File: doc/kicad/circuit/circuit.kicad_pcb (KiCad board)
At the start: 2 copper layers, 45.5 x 53.1 mm, 17 parts, among them J1 4X4 Button Matrix, J1.1 2X2 Button Matrix A, J1.1.1 Button 1, J1.1.2 Button 2, J1.1.3 Button 5, J1.1.4 Button 6, J1.2 2X2 Button Matrix B, J1.2.1 Button 3, J1.2.2 Button 4, J1.3 2X2 Button Matrix C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

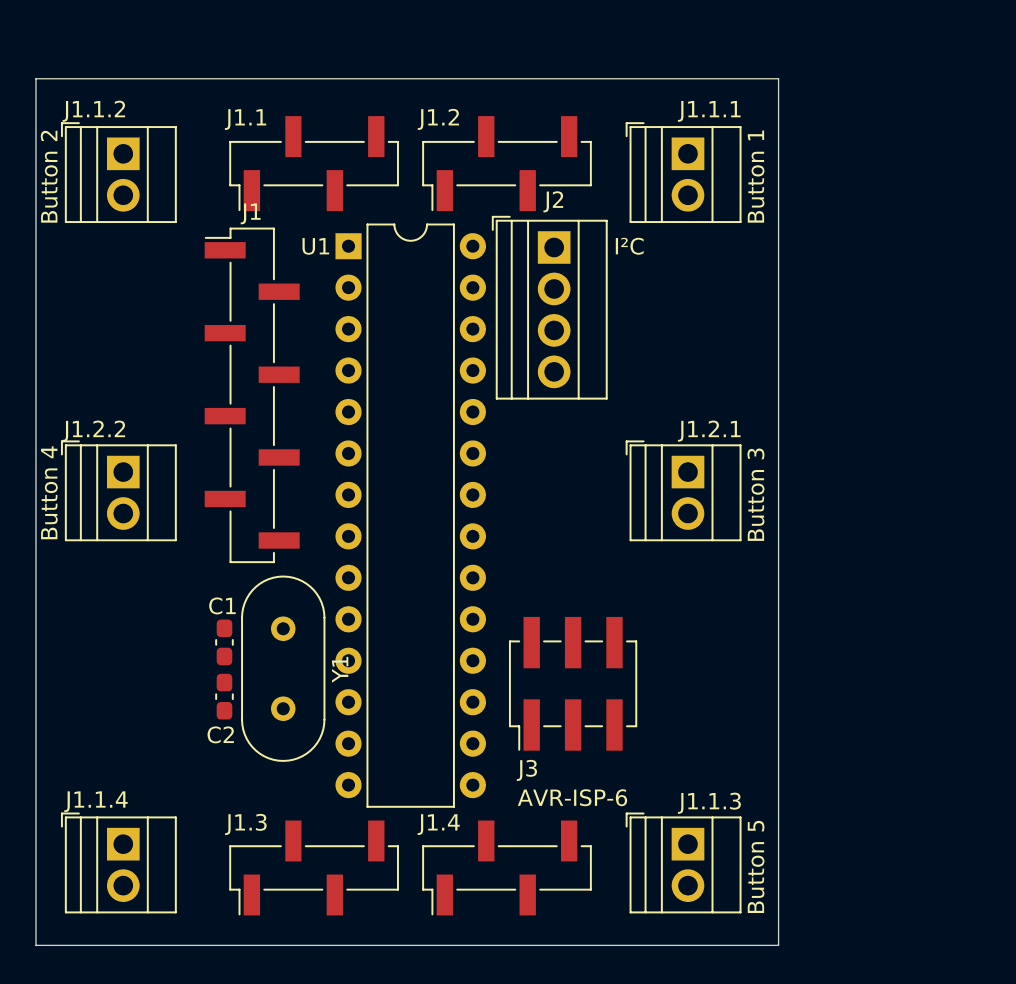
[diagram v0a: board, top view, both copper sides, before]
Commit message: first test runs good in arduino uno envirement
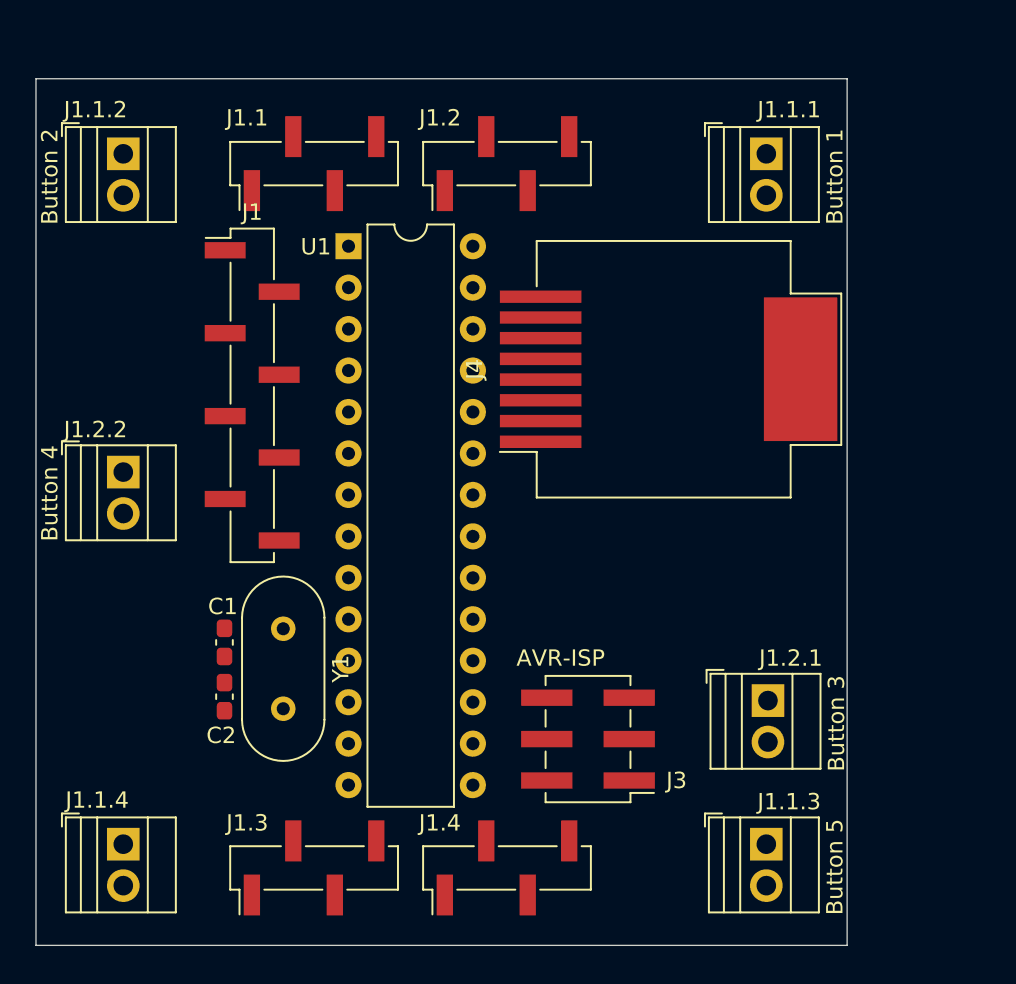
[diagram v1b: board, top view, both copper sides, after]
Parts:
- removed J2: I²C, TerminalBlock:TerminalBlock_Xinya_XY308-2.54-4P_1x04_P2.54mm_Horizontal
- added J4: RJ45, Connector_RJ:RJ45_Molex_0855135013_Vertical, F.Cu at (240.8, 63.0)
- J1: value 4X4 Button Matrix -> 4X4 Button Matrix
- J3: value AVR-ISP-6 -> AVR-ISP
- moved J1.2.1 14.8 mm to (246.9, 83.3)
- moved J1.1.1 4.80 mm to (246.8, 49.8)
- moved J1.1.3 4.80 mm to (246.8, 92.1)
- moved J3 3.51 mm to (235.9, 85.7), turned to 180 degrees
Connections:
- net Net-(J3-MISO) renamed /MISO
- net Net-(J3-MOSI) renamed /MOSI
- net Net-(J3-SCK) renamed /SCK
- net Net-(J3-~{RST}) renamed /RESET
- net Net-(U1-XTAL1/PB6) renamed /XTAL1
- net Net-(U1-XTAL2/PB7) renamed /XTAL2
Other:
- board size 45.5 x 53.1 mm -> 49.7 x 53.1 mm

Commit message: add some comments and update pcb
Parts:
- added REF**: MountingHole_2.2mm_M2, MountingHole:MountingHole_2.2mm_M2, F.Cu at (249.0, 77.3)
- added REF**: MountingHole_2.2mm_M2, MountingHole:MountingHole_2.2mm_M2, F.Cu at (204.8, 57.0)
- added REF**: MountingHole_2.2mm_M2, MountingHole:MountingHole_2.2mm_M2, F.Cu at (204.8, 86.1)
- added REF**: MountingHole_2.2mm_M2, MountingHole:MountingHole_2.2mm_M2, F.Cu at (239.8, 47.9)
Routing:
- net /L1: track 0.00 -> 122.1 mm
- net /R2: track 0.00 -> 119.2 mm, vias 0 -> 3
- net /R1: track 0.00 -> 113.9 mm, vias 0 -> 2
- net /L3: track 0.00 -> 81.1 mm
- net /L2: track 0.00 -> 80.0 mm, vias 0 -> 1
- net /R3: track 0.00 -> 70.8 mm
- net /L4: track 0.00 -> 69.9 mm, vias 0 -> 1
- net GND: track 0.00 -> 53.1 mm, vias 0 -> 4
- net /RESET: track 0.00 -> 48.1 mm, vias 0 -> 1
- net +5V: track 0.00 -> 42.7 mm
- net /R4: track 0.00 -> 36.5 mm
- net /MISO: track 0.00 -> 14.6 mm
- net /SCK: track 0.00 -> 13.8 mm
- net /XTAL2: track 0.00 -> 10.8 mm
- net /XTAL1: track 0.00 -> 8.90 mm
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- added copper zone on F.Cu, net +5V
- added copper zone on B.Cu, net GND

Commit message: finish PCBA
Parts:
- added SW1: Reset, Button_Switch_SMD:SW_Push_1P1T_NO_6x6mm_H9.5mm, F.Cu at (238.8, 76.2)
- J1.1: value 2X2 Button Matrix A -> 2X2 Matrix A
- J1.2: value 2X2 Button Matrix B -> 2X2 Matrix B
- J1.3: value 2X2 Button Matrix C -> 2X2 Matrix C
- J1.4: value 2X2 Button Matrix D -> 2X2 Matrix D
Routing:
- net GND: track 53.1 -> 28.5 mm, vias 4 -> 1
- net /RESET: track 48.1 -> 57.8 mm
- net /R2: track 119.2 -> 127.6 mm
- net /L1: track 122.1 -> 116.9 mm, vias 0 -> 1
- net /L3: track 81.1 -> 86.1 mm
- net /L4: track 69.9 -> 73.5 mm
- net /R1: track 113.9 -> 115.2 mm
- net +5V: track 42.7 -> 42.0 mm, vias 0 -> 2
- added copper zone on B.Cu, net +5V
- added copper zone on F.Cu, net GND
- removed copper zone on F.Cu, net +5V
- removed copper zone on B.Cu, net GND

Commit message: refactor pcb
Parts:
- C1, C2: footprint Capacitor_SMD:C_0603_1608Metric_Pad1.08x0.95mm_HandSolder -> Capacitor_SMD:C_0402_1005Metric
- J1: footprint Connector_PinHeader_2.54mm:PinHeader_1x08_P2.54mm_Vertical_SMD_Pin1Left -> Connector_PinHeader_2.54mm:PinHeader_2x04_P2.54mm_Vertical_SMD
- J1.1: value 2X2 Matrix A -> 2X2 Button Matrix A; footprint Connector_PinHeader_2.54mm:PinHeader_1x04_P2.54mm_Vertical_SMD_Pin1Left -> Connector_PinHeader_2.54mm:PinHeader_2x02_P2.54mm_Vertical_SMD
- J1.2: value 2X2 Matrix B -> 2X2 Button Matrix B; footprint Connector_PinHeader_2.54mm:PinHeader_1x04_P2.54mm_Vertical_SMD_Pin1Left -> Connector_PinHeader_2.54mm:PinHeader_2x02_P2.54mm_Vertical_SMD
- J1.3: value 2X2 Matrix C -> 2X2 Button Matrix C; footprint Connector_PinHeader_2.54mm:PinHeader_1x04_P2.54mm_Vertical_SMD_Pin1Left -> Connector_PinHeader_2.54mm:PinHeader_2x02_P2.54mm_Vertical_SMD
- J1.4: value 2X2 Matrix D -> 2X2 Button Matrix D; footprint Connector_PinHeader_2.54mm:PinHeader_1x04_P2.54mm_Vertical_SMD_Pin1Left -> Connector_PinHeader_2.54mm:PinHeader_2x02_P2.54mm_Vertical_SMD
- moved C1 10.9 mm to (221.8, 72.6)
- moved Y1 10.4 mm to (225.2, 72.1)
- moved C2 10.4 mm to (221.8, 76.7)
- moved J1 9.07 mm to (222.1, 58.6)
- moved SW1 8.43 mm to (246.7, 73.3)
- moved J1.1.1 8.43 mm to (254.8, 47.0)
- moved J1.1.2 8.43 mm to (215.3, 47.0)
- moved J1.1.3 8.43 mm to (254.8, 89.3)
- moved J1.1.4 8.43 mm to (215.3, 89.3)
- moved J1.2.1 8.43 mm to (254.8, 80.5)
- moved J1.2.2 8.43 mm to (215.3, 66.5)
- moved J3 8.43 mm to (243.8, 82.9)
- moved J4 8.43 mm to (248.8, 60.2)
- moved REF** 8.43 mm to (256.9, 74.5)
- moved REF** 8.43 mm to (212.8, 54.2)
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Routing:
- net /R2: track 127.6 -> 178.0 mm, vias 3 -> 0
- net +5V: track 42.0 -> 1.27 mm
- net /R1: track 115.2 -> 151.3 mm, vias 2 -> 0
- net /L1: track 116.9 -> 147.1 mm, vias 1 -> 0
- net GND: track 28.5 -> 0.00 mm, vias 1 -> 0
- net /R4: track 36.5 -> 54.2 mm
- net /L2: track 80.0 -> 96.7 mm, vias 1 -> 0
- net /L4: track 73.5 -> 81.7 mm
- net /L3: track 86.1 -> 92.1 mm
- net /R3: track 70.8 -> 65.1 mm
- net /XTAL2: track 10.8 -> 7.98 mm
- net /XTAL1: track 8.90 -> 7.73 mm
- net /SCK: track 13.8 -> 14.9 mm
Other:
- board text added: "github.com/lusmdl/MySimRacingWheeleButtons"
